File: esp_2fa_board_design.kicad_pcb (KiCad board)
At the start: 2 copper layers, 82 x 45 mm, 53 parts, among them IC1 TPS22919DCKR, J1 Conn_01x02_Female, J2 TYPE-C-31-M-17, J3 Conn_01x02_Female, Q1 DMP2305U-7, SW1 SW_Push, SW2 SW_Push, SW3 BOOT, SW4 RESET, SW5 POWER SWITCH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

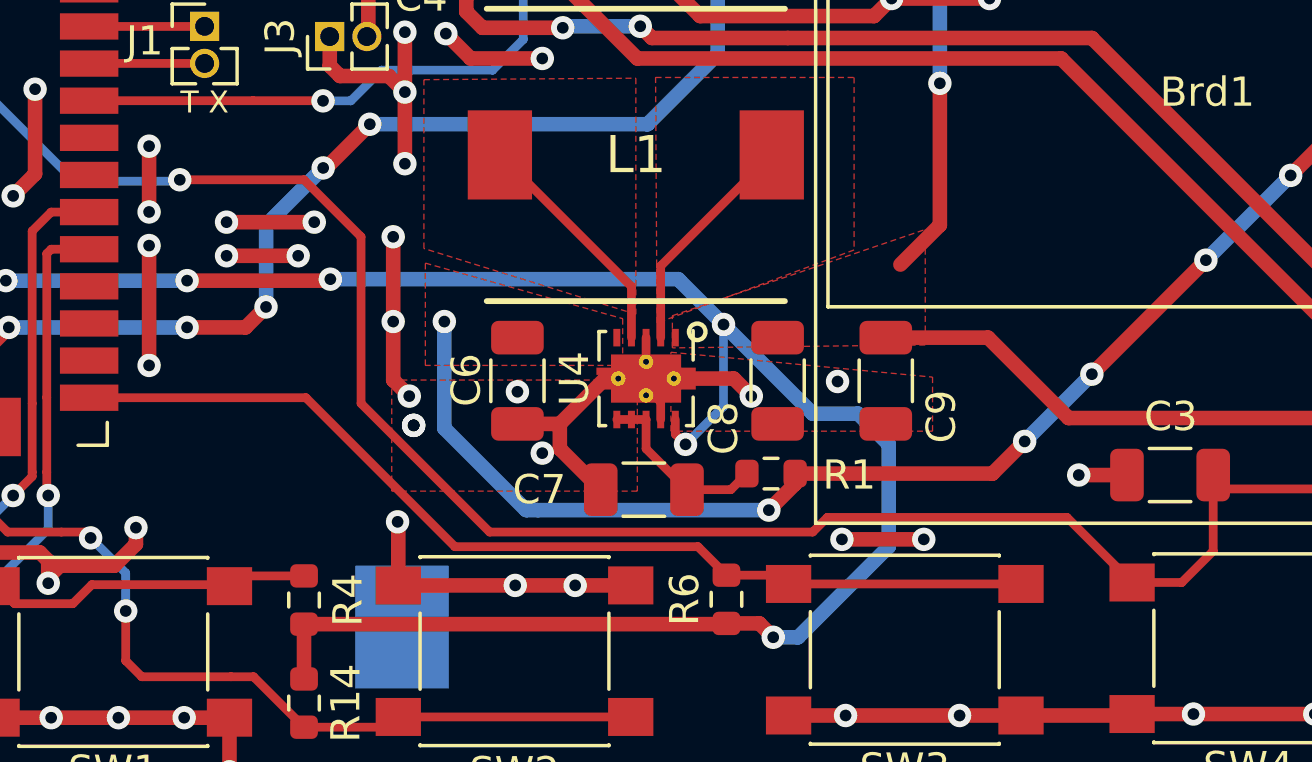
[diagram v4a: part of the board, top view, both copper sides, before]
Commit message: Updated schematics by adding one more filter capacitor to voltage regulator VIN and changed routing accordingly
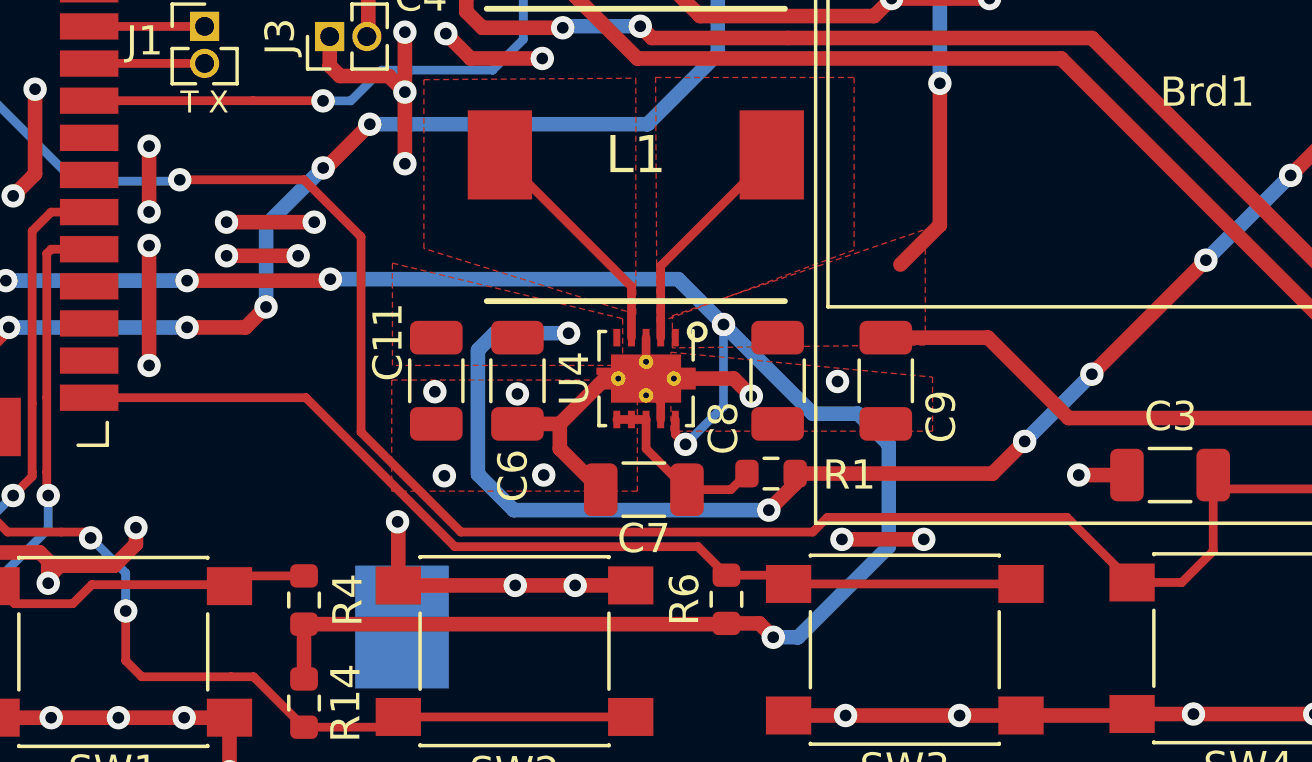
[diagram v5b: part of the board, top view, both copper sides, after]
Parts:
- added C11: 10uF 50V, Capacitor_SMD:C_1206_3216Metric, F.Cu at (124.3, 103.6)
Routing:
- net GND: track 242.5 -> 236.8 mm, vias 71 -> 68
- net Net-(C11-Pad1): track 55.3 -> 57.5 mm
- net /EN: track 78.9 -> 79.5 mm

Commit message: Completed routing pcb
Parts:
- removed the REF** at (120.4, 56.1)
- added REF**: OSHW-Logo2_9.8x8mm_SilkScreen, Symbol:OSHW-Logo2_9.8x8mm_SilkScreen, B.Cu at (156.1, 102.3)
- DOWN: renamed from SW2; value SW_Push -> DOWN
- SELECT: renamed from SW3; value BOOT -> BOOT/SELECT
- TP1, TP2, TP3, TP4, TP5, TP6, TP7, TP8: moved to B.Cu
- UP: renamed from SW1; value SW_Push -> UP
- moved TP2 55.0 mm to (119.8, 119.3)
- moved TP3 54.9 mm to (121.5, 119.3)
- moved TP5 32.1 mm to (161.2, 93.5)
- moved TP8 30.4 mm to (144.5, 99.6)
- moved REF** 27.9 mm to (156.5, 109.8)
- moved TP1 25.5 mm to (144.5, 96.5)
- moved TP6 23.8 mm to (161.0, 82.9)
- moved TP7 22.3 mm to (158.8, 82.9)
- moved TP4 17.2 mm to (163.3, 82.9)
- renumbered SW4 to RESET
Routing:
- net GND: track 236.8 -> 296.4 mm, vias 68 -> 101
- net /IO18_SCL: track 28.3 -> 50.2 mm, vias 2 -> 3
- net /IO5_SDA: track 28.4 -> 49.6 mm, vias 2 -> 3
- net /LOAD_SWITCH_VCC: track 101.6 -> 119.4 mm, vias 10 -> 8
- net /IO21_SDA: track 48.0 -> 58.6 mm
- net /IO22_SCL: track 47.1 -> 55.5 mm
- net +3V3: track 135.8 -> 142.9 mm
- net /V_INPUT: track 18.0 -> 24.9 mm
- net Net-(C11-Pad1): track 57.5 -> 59.2 mm
- net /IO25: track 48.1 -> 47.1 mm
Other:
- board size 82 x 45 mm -> 82 x 42 mm
- board text added: "+"
- board text added: "SCL"
- board text added: "SDA"
- board text added: "VCC"
- board text added: "v1.3 Vedant Paranjape"
- board text removed: "v1.2 Vedant Paranjape"

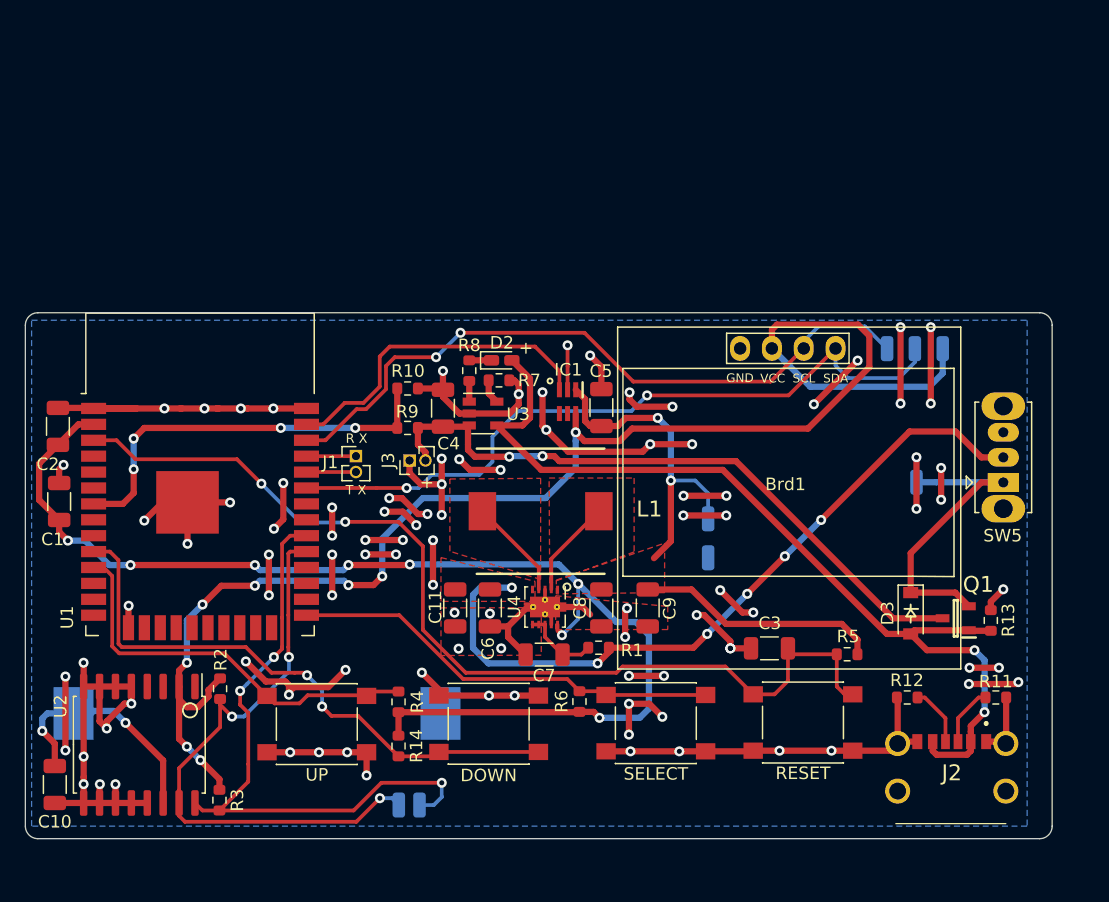
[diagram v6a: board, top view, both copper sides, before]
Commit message: Changed thermal via sizes to match manufacturer specs
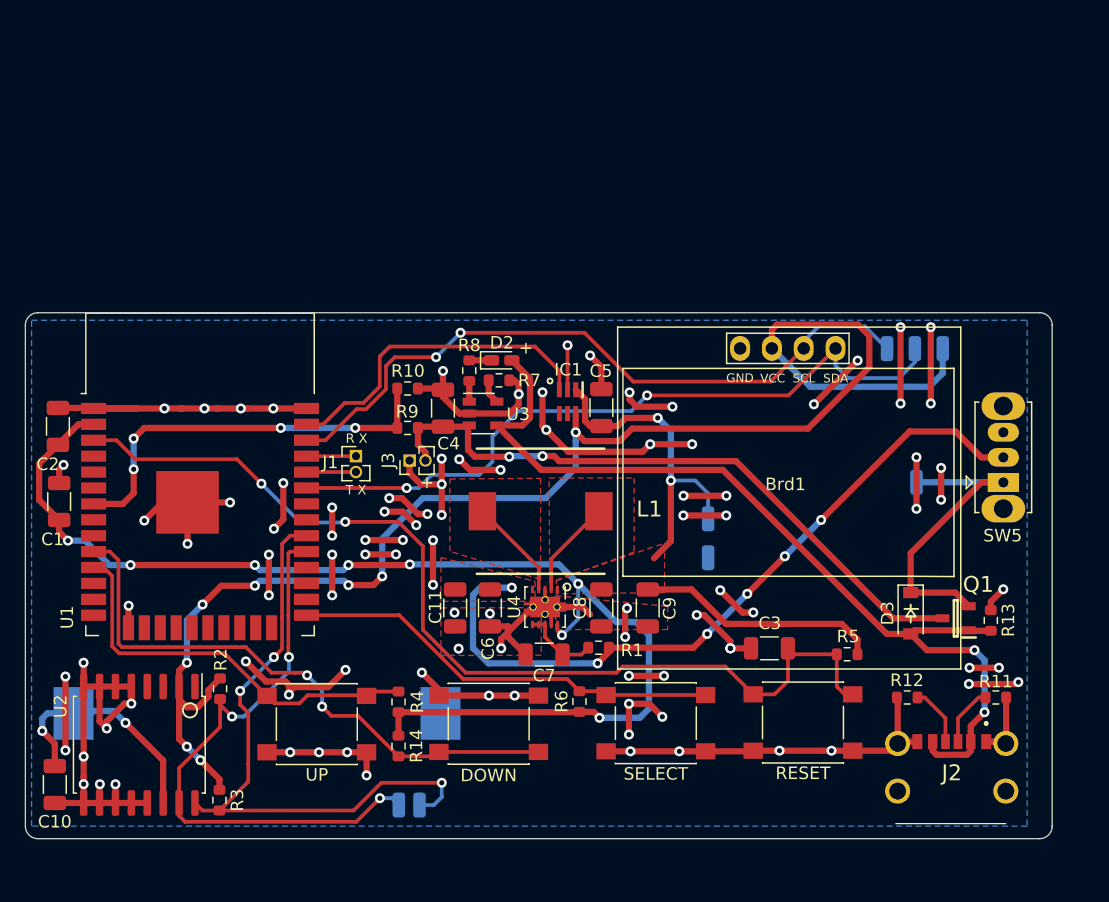
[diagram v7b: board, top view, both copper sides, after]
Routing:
- net GND: track 296.4 -> 298.1 mm
